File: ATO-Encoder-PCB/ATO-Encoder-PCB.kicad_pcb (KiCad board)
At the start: 2 copper layers, 82.6 x 92.5 mm, 31 parts, among them IC1 MCP2561-H_P, IC3 MCP2561-H_P, J1 DE9_Socket, J2 Conn_01x06, J3 B2B-XH-A, J4 B2B-XH-A, J5 B2B-XH-A, J6 B2B-XH-A

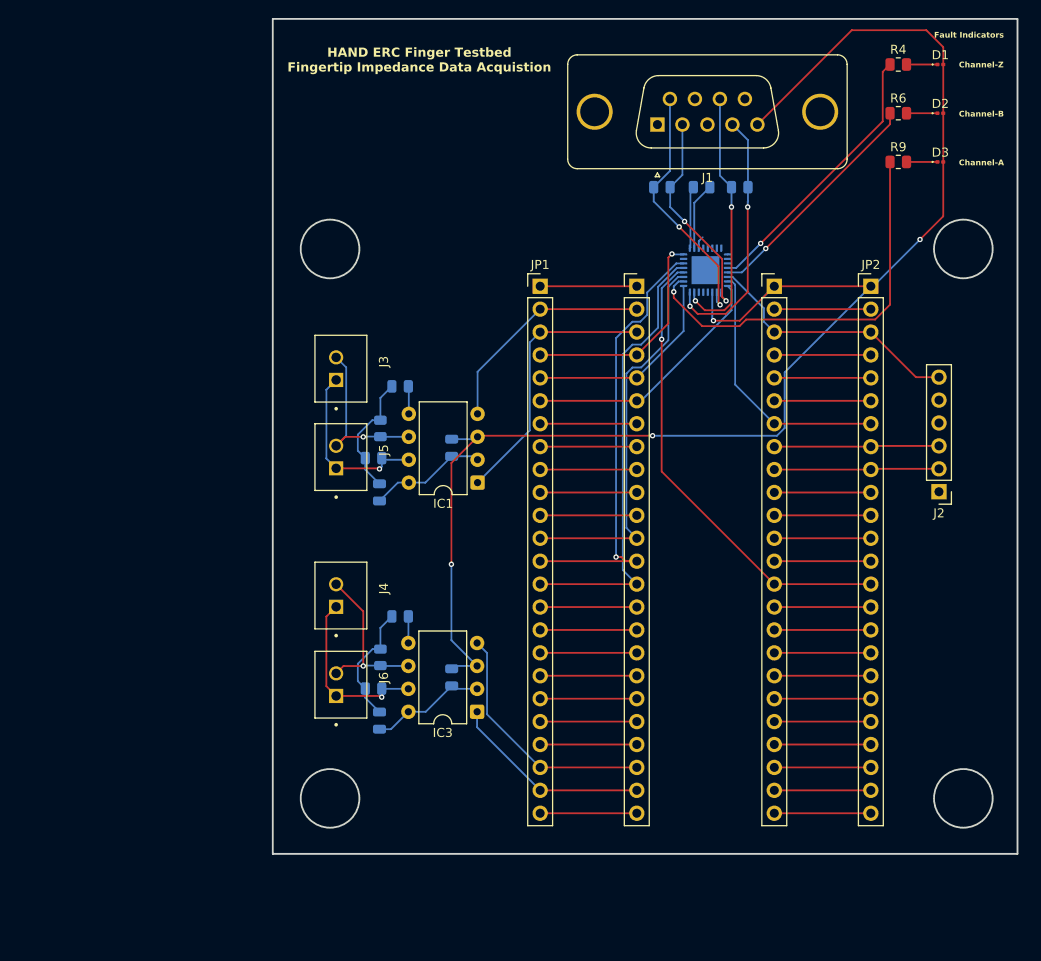
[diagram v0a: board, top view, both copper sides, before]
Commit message: Shrunk the board outline
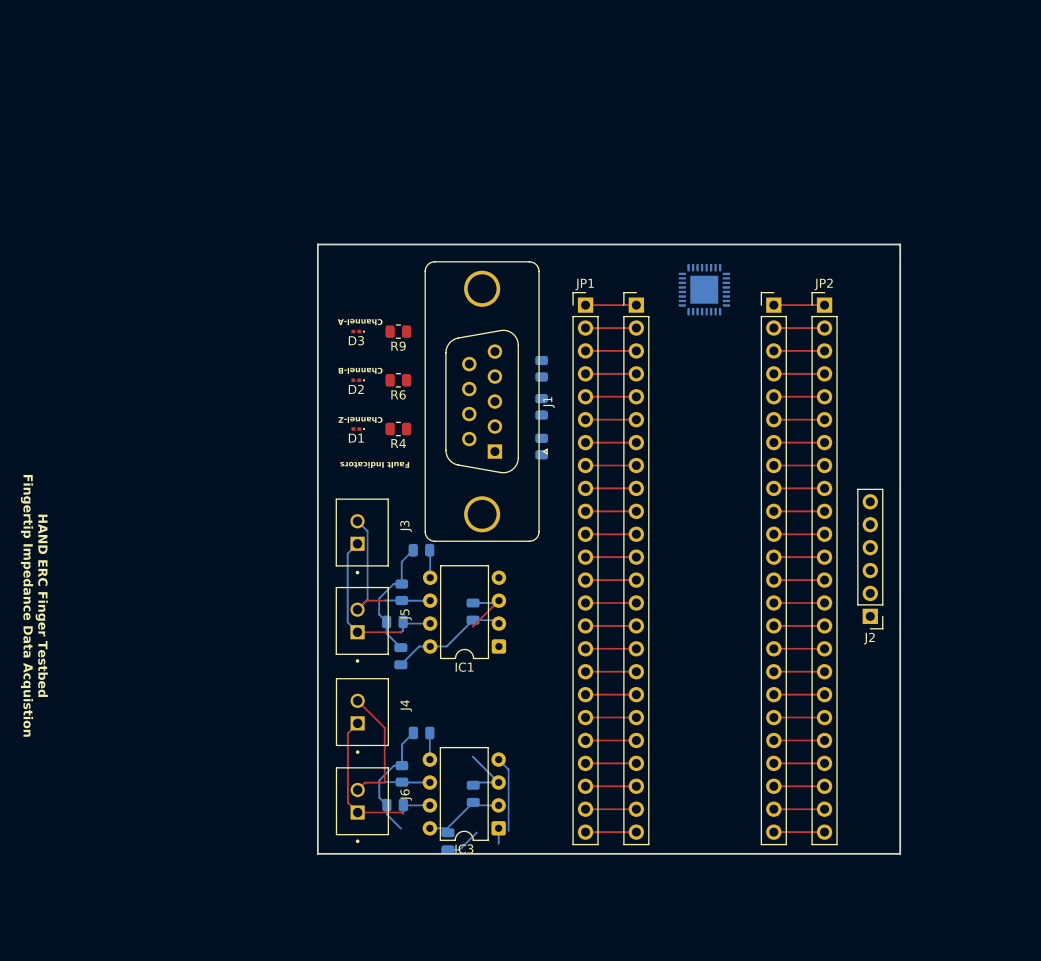
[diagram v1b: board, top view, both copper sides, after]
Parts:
- moved D1 76.3 mm to (132.0, 68.4), turned to 180 degrees
- moved D2 71.2 mm to (132.0, 63.0), turned to 180 degrees
- moved R4 68.6 mm to (136.7, 68.4), turned to 180 degrees
- moved D3 67.4 mm to (132.0, 57.6), turned to 180 degrees
- moved R6 62.8 mm to (136.7, 63.0), turned to 180 degrees
- moved R9 58.5 mm to (136.7, 57.6), turned to 180 degrees
- moved J1 41.3 mm to (145.5, 65.4), turned to -90 degrees
- moved R1 31.7 mm to (152.6, 70.4), turned to 90 degrees
- moved R2 30.1 mm to (152.6, 66.0), turned to 90 degrees
- moved R3 29.8 mm to (152.6, 61.7), turned to -90 degrees
- moved R5 18.3 mm to (139.2, 81.8)
- moved IC1 18.3 mm to (144.0, 88.4)
- moved R7 18.3 mm to (136.3, 89.8)
- moved R8 18.3 mm to (137.0, 86.5)
- moved C1 18.3 mm to (144.9, 88.6)
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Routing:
- net +5V: track 167.7 -> 19.9 mm, vias 4 -> 0
- net CLK: track 51.8 -> 5.62 mm, vias 1 -> 0
- net Net-(U1-~{AFAULT}): track 44.7 -> 0.00 mm, vias 1 -> 0
- net SDO: track 50.2 -> 5.63 mm
- net SDI: track 49.8 -> 5.63 mm, vias 1 -> 0
- net CS: track 43.7 -> 5.63 mm
- net Net-(U1-~{ZFAULT}): track 30.6 -> 0.00 mm, vias 1 -> 0
- net Net-(U1-~{A}): track 28.9 -> 0.00 mm, vias 2 -> 0
- net Net-(U1-A): track 28.6 -> 0.00 mm, vias 2 -> 0
- net /3v3: track 39.6 -> 11.3 mm
- net Net-(U1-~{Z}): track 28.2 -> 0.00 mm, vias 2 -> 0
- net Net-(U1-~{BFAULT}): track 26.0 -> 0.00 mm, vias 1 -> 0
- net /CTX2: track 30.3 -> 5.63 mm
- net Net-(U1-Z): track 24.3 -> 0.00 mm, vias 2 -> 0
- net SPI: track 28.9 -> 5.62 mm
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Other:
- board size 82.6 x 92.5 mm -> 64.6 x 67.5 mm

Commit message: PBC is ready for manufacture
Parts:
- removed the C1 at (144.9, 88.6)
- removed the C2 at (136.9, 93.6)
- removed the IC1 at (144.0, 88.4)
- removed the J3 at (132.7, 79.9)
- removed the R5 at (139.2, 81.8)
- removed the R7 at (136.3, 89.8)
- removed the R8 at (137.0, 86.5)
- added C3: 3.3uF, Capacitor_SMD:C_0805_2012Metric, B.Cu at (172.1, 55.8)
- added C4: 3.3uF, Capacitor_SMD:C_0805_2012Metric, B.Cu at (169.5, 88.2)
- added D4: LED, LED_THT:LED_D3.0mm, F.Cu at (155.5, 56.7)
- added R10: 150R, Resistor_SMD:R_0805_2012Metric, F.Cu at (154.6, 53.0)
- D1, D2, D3: footprint LED_SMD:LED_0201_0603Metric -> LED_THT:LED_D3.0mm
- J5: value B2B-XH-A -> Screw_Terminal_01x02; footprint BoardToCable_2PinMale:JST_B2B-XH-A -> TerminalBlock:TerminalBlock_MaiXu_MX126-5.0-02P_1x02_P5.00mm
- R4, R6, R9: value 330R -> 150R; moved to B.Cu
- moved D3 45.6 mm to (150.5, 99.3), turned to 0 degrees
- moved R9 42.1 mm to (151.9, 96.8)
- moved J5 37.7 mm to (148.0, 55.2), turned to 180 degrees
- moved D2 36.0 mm to (150.5, 93.9), turned to 0 degrees
- moved U1 32.5 mm to (151.7, 79.4), turned to -90 degrees
- moved R6 32.2 mm to (151.9, 91.4)
- moved D1 27.3 mm to (150.5, 88.5), turned to 0 degrees
- moved R4 23.3 mm to (151.9, 86.0)
- moved R1 14.2 mm to (145.5, 82.7), turned to -90 degrees
- moved R2 14.0 mm to (145.6, 78.1)
- moved R3 14.0 mm to (145.6, 73.8)
- moved J1 14.0 mm to (138.5, 77.5)
- moved C2 3.00 mm to (139.2, 113.5)
- moved J4 2.43 mm to (190.5, 89.0)
- moved JP1 2.43 mm to (158.9, 51.0)
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- renumbered C3 to C1, C8 to C2, IC3 to IC1, J6 to J2, J4 to J3, J2 to J4, R10 to R5, R11 to R7, R12 to R8
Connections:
- J5 pad 1: /CANH2 -> +5V
- J5 pad 2: /CANL2 -> GND
- JP1 pad 10: Net-(U$1-P8/PWM/IN1/TX2) -> Encoder Fault
- JP1 pad 17: Net-(U$1-P25/PWM/SDA2/RX6/A11) -> ZO
- JP1 pad 18: Net-(U$1-P26/MOSI1/A12) -> SPI
- JP1 pad 4: BO -> Net-(U$1-P2/PWM/OUT2)
- JP1 pad 5: AO -> Net-(U$1-P3/PWM/LRCLK2)
- JP1 pad 6: ZO -> Net-(U$1-P4/PWM/BCLK2)
- JP1 pad 8: Net-(U$1-P6/PWM/OUT1D) -> AO
- JP1 pad 9: Net-(U$1-P7/PWM/OUT1A/RX2) -> BO
- JP2 pad 7: SPI -> Net-(U$1-LRCLK1/TX5/A6/P20)
- U$1 pad P16: Net-(U$1-P25/PWM/SDA2/RX6/A11) -> ZO
- U$1 pad P17: Net-(U$1-P26/MOSI1/A12) -> SPI
- U$1 pad P3: BO -> Net-(U$1-P2/PWM/OUT2)
- U$1 pad P4: AO -> Net-(U$1-P3/PWM/LRCLK2)
- U$1 pad P41: SPI -> Net-(U$1-LRCLK1/TX5/A6/P20)
- U$1 pad P5: ZO -> Net-(U$1-P4/PWM/BCLK2)
- U$1 pad P7: Net-(U$1-P6/PWM/OUT1D) -> AO
- U$1 pad P8: Net-(U$1-P7/PWM/OUT1A/RX2) -> BO
- U$1 pad P9: Net-(U$1-P8/PWM/IN1/TX2) -> Encoder Fault
- U1 pad 12: unconnected-(U1-LO2-Pad12) -> (no net)
- U1 pad 13: unconnected-(U1-DI2-Pad13) -> (no net)
- U1 pad 15: unconnected-(U1-~{Y}-Pad15) -> (no net)
- U1 pad 16: unconnected-(U1-DIY-Pad16) -> (no net)
- U1 pad 19: unconnected-(U1-~{YFAULT}-Pad19) -> (no net)
- U1 pad 28: unconnected-(U1-LO3-Pad28) -> (no net)
- U1 pad 29: unconnected-(U1-DI3-Pad29) -> (no net)
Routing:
- net +5V: track 19.9 -> 81.9 mm, vias 0 -> 1
- net Net-(U1-~{AFAULT}): track 0.00 -> 54.5 mm, vias 0 -> 2
- net /3v3: track 11.3 -> 54.3 mm, vias 0 -> 1
- net CLK: track 5.62 -> 39.7 mm
- net Net-(U1-~{B}): track 0.00 -> 23.3 mm, vias 0 -> 2
- net ZO: track 5.63 -> 26.3 mm, vias 0 -> 1
- net SPI: track 5.62 -> 26.3 mm, vias 0 -> 1
- net /CANL2: track 20.6 -> 0.00 mm
- net /CANH2: track 19.9 -> 0.00 mm
- net Net-(U1-B): track 0.00 -> 19.8 mm, vias 0 -> 3
- net SDO: track 5.63 -> 22.5 mm, vias 0 -> 1
- net CS: track 5.63 -> 20.2 mm, vias 0 -> 1
- net Net-(U1-~{A}): track 0.00 -> 14.2 mm
- net SDI: track 5.63 -> 19.7 mm
- net Net-(C2-Pad2) (its old number): track 13.9 -> 0.00 mm
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- added copper zone on F.Cu, net +5V
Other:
- board size 64.6 x 67.5 mm -> 66.2 x 80.8 mm
- rule pad_to_mask_clearance: 0 -> 0.0508
- board text added: "+"
- board text added: "A"
- board text added: "B"
- board text added: "Z"
- board text removed: "Channel-A"
- board text removed: "Channel-B"
- board text removed: "Channel-Z"
- board text removed: "HAND ERC Finger Testbed Fingertip Impedance Data Acquistion"

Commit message: Order has been placed with OSH Park
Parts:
- added G***: LOGO, Teensy4.1:HAND_Logo, F.Cu at (181.5, 119.5)
- renumbered C4 to C3, C3 to C4
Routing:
- net +5V: track 81.9 -> 122.2 mm
- net GND: track 33.6 -> 25.2 mm
- added copper zone on B.Cu, net GND
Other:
- board text added: "+5V"
- board text added: "-"
- board text added: "Designed By: Tony Shilati"
- board text added: "H"
- board text added: "HAND ERC Finger Testbed Fingertip Impedance Data Acquisition"
- board text added: "L"
